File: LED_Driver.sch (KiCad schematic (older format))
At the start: 6 parts

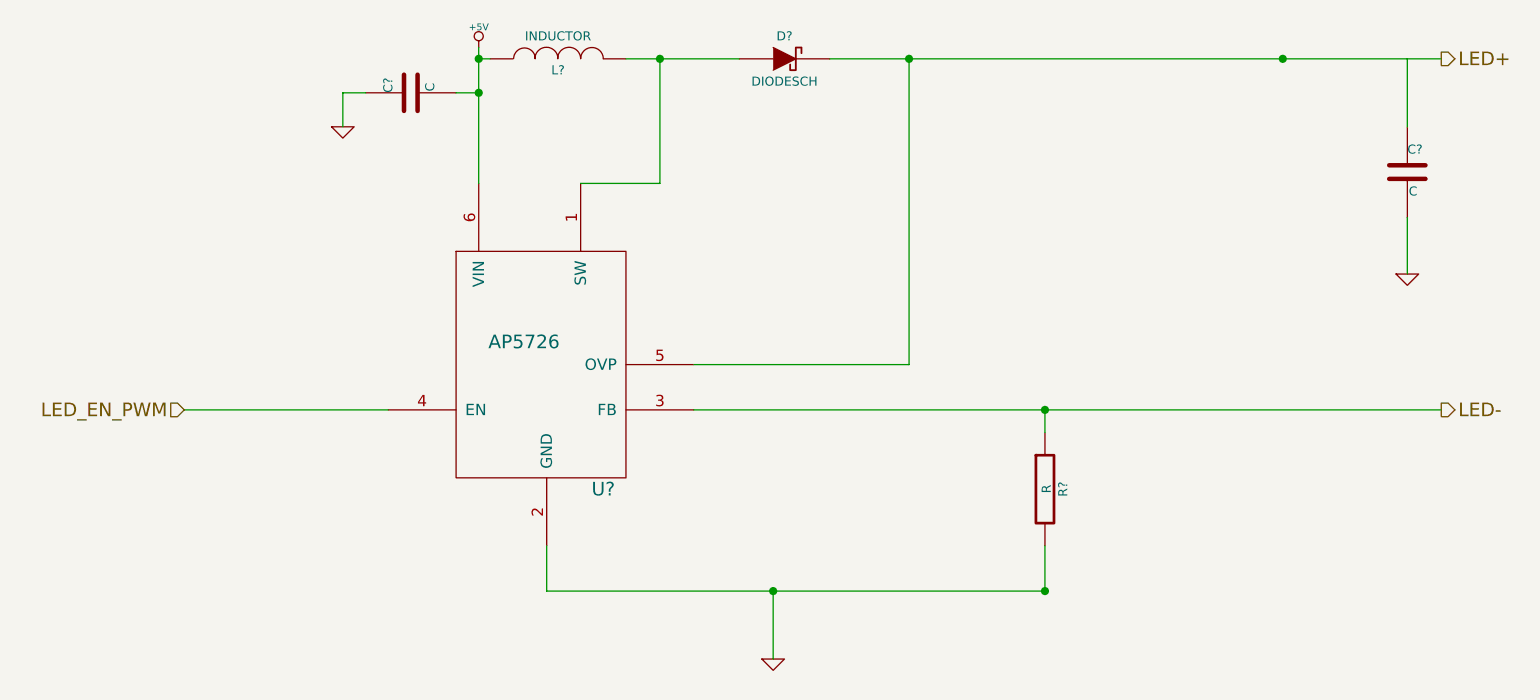
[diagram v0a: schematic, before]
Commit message: RELAY 02-20-2014
1) Created and associated footprints for relay module
2) Placed relay module's components in PCB layout
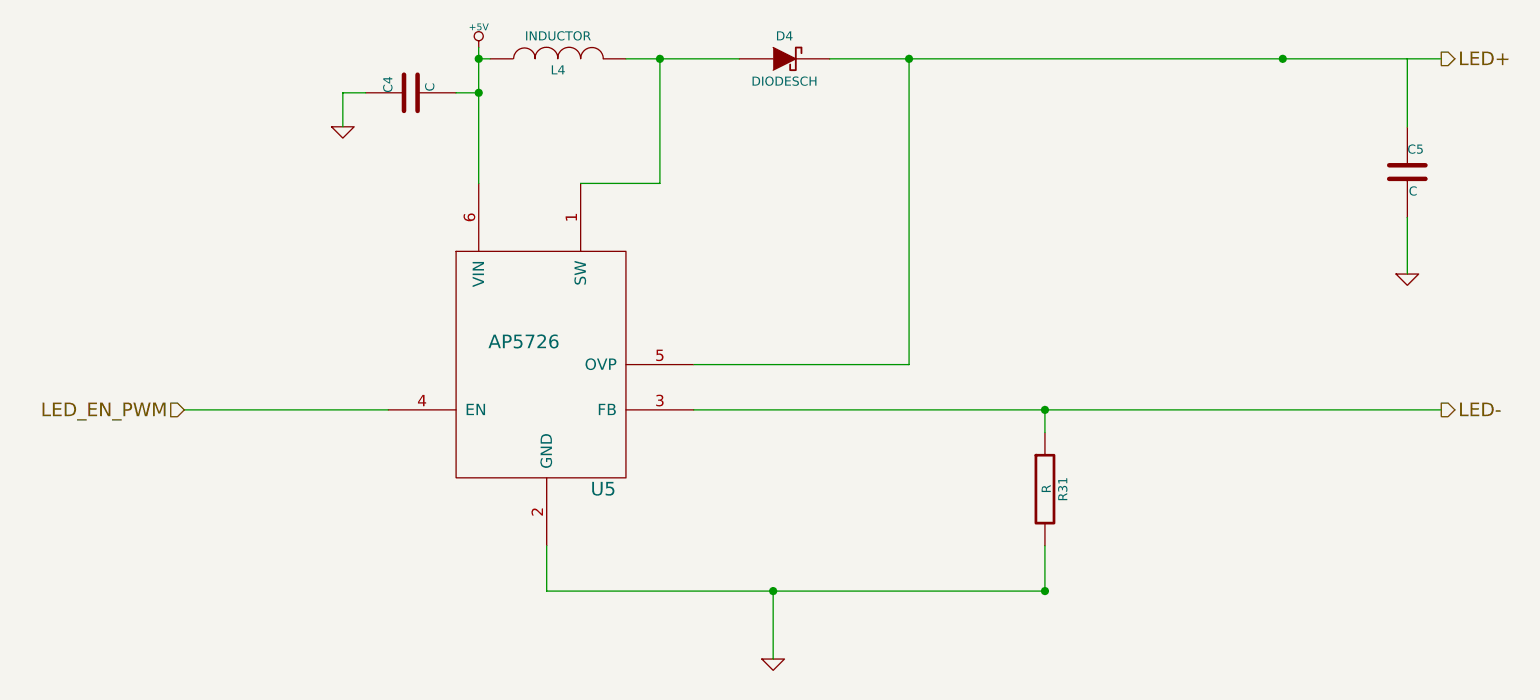
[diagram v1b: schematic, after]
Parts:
- gave numbers to parts that had none: 6
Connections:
- wire segments 27 -> 20
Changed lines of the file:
@@
 Sheet 5 9
 Title ""
-Date "11 feb 2014"
+Date "20 feb 2014"
 Rev ""
 Comp ""
@@
 LED-
 $Comp
-L AP5726 U?
+L AP5726 U5
 U 1 1 52F8483D
 P 4600 2800
-F 0 "U?" H 4950 2350 60  0000 C CNN
+F 0 "U5" H 4950 2350 60  0000 C CNN
 F 1 "AP5726" H 4600 3000 60  0000 C CNN
 F 2 "" H 4600 2800 60  0000 C CNN
@@
 	3100 2900 4000 2900
 $Comp
-L +5V #PWR?
+L +5V #PWR34
 U 1 1 52F84ACD
 P 4400 1300
-F 0 "#PWR?" H 4400 1390 20  0001 C CNN
+F 0 "#PWR34" H 4400 1390 20  0001 C CNN
 F 1 "+5V" H 4400 1390 30  0000 C CNN
 F 2 "" H 4400 1300 60  0000 C CNN
@@
 $EndComp
 $Comp
-L GND #PWR?
+L GND #PWR33
 U 1 1 52F84ADC
 P 3800 1650
-F 0 "#PWR?" H 3800 1650 30  0001 C CNN
+F 0 "#PWR33" H 3800 1650 30  0001 C CNN
 F 1 "GND" H 3800 1580 30  0001 C CNN
 F 2 "" H 3800 1650 60  0000 C CNN
@@
 $EndComp
 Wire Wire Line
-	4400 1300 4400 1350
-Wire Wire Line
-	4400 1350 4400 1500
-Wire Wire Line
-	4400 1500 4400 1900
+	4400 1300 4400 1900
 $Comp
-L C C?
+L C C4
 U 1 1 52F84B01
 P 4100 1500
-F 0 "C?" H 4100 1600 40  0000 L CNN
+F 0 "C4" H 4100 1600 40  0000 L CNN
 F 1 "C" H 4106 1415 40  0000 L CNN
 F 2 "~" H 4138 1350 30  0000 C CNN
@@
 	3800 1500 3800 1650
 $Comp
-L INDUCTOR L?
+L INDUCTOR L4
 U 1 1 52F84B22
 P 4750 1350
-F 0 "L?" V 4700 1350 40  0000 C CNN
+F 0 "L4" V 4700 1350 40  0000 C CNN
 F 1 "INDUCTOR" V 4850 1350 40  0000 C CNN
 F 2 "~" H 4750 1350 60  0000 C CNN
@@
 Connection ~ 4400 1350
 Wire Wire Line
-	5050 1350 5200 1350
-Wire Wire Line
-	5200 1350 5550 1350
+	5050 1350 5550 1350
 Wire Wire Line
 	5200 1350 5200 1900
@@
 	5200 1900 4850 1900
 $Comp
-L DIODESCH D?
+L DIODESCH D4
 U 1 1 52F84B4A
 P 5750 1350
-F 0 "D?" H 5750 1450 40  0000 C CNN
+F 0 "D4" H 5750 1450 40  0000 C CNN
 F 1 "DIODESCH" H 5750 1250 40  0000 C CNN
 F 2 "~" H 5750 1350 60  0000 C CNN
@@
 	6300 2700 6300 1350
 Wire Wire Line
-	5950 1350 6300 1350
-Wire Wire Line
-	6300 1350 7950 1350
-Wire Wire Line
-	7950 1350 8650 1350
+	5950 1350 8650 1350
 $Comp
-L R R?
+L R R31
 U 1 1 52F84B73
 P 6900 3250
-F 0 "R?" V 6980 3250 40  0000 C CNN
+F 0 "R31" V 6980 3250 40  0000 C CNN
 F 1 "R" V 6907 3251 40  0000 C CNN
 F 2 "~" V 6830 3250 30  0000 C CNN
@@
 $EndComp
 Wire Wire Line
-	5350 2900 6900 2900
-Wire Wire Line
-	6900 2900 8650 2900
+	5350 2900 8650 2900
 Wire Wire Line
 	6900 2900 6900 3000
@@
 	6900 3700 6900 3500
 $Comp
-L C C?
+L C C5
 U 1 1 52F84BA7
 P 8500 1850
-F 0 "C?" H 8500 1950 40  0000 L CNN
+F 0 "C5" H 8500 1950 40  0000 L CNN
 F 1 "C" H 8506 1765 40  0000 L CNN
 F 2 "~" H 8538 1700 30  0000 C CNN
@@
 Connection ~ 6300 1350
 $Comp
-L GND #PWR?
+L GND #PWR35
 U 1 1 52F84BE2
 P 5700 4000
-F 0 "#PWR?" H 5700 4000 30  0001 C CNN
+F 0 "#PWR35" H 5700 4000 30  0001 C CNN
 F 1 "GND" H 5700 3930 30  0001 C CNN
 F 2 "" H 5700 4000 60  0000 C CNN
@@
 Connection ~ 7950 1350
 $Comp
-L GND #PWR?
+L GND #PWR36
 U 1 1 52F84C43
 P 8500 2300
-F 0 "#PWR?" H 8500 2300 30  0001 C CNN
+F 0 "#PWR36" H 8500 2300 30  0001 C CNN
 F 1 "GND" H 8500 2230 30  0001 C CNN
 F 2 "" H 8500 2300 60  0000 C CNN
@@
 	8500 2300 8500 2050
 Wire Wire Line
-	4700 3700 5700 3700
-Wire Wire Line
-	5700 3700 6900 3700
+	4700 3700 6900 3700
 Connection ~ 6900 2900
 $EndSCHEMATC

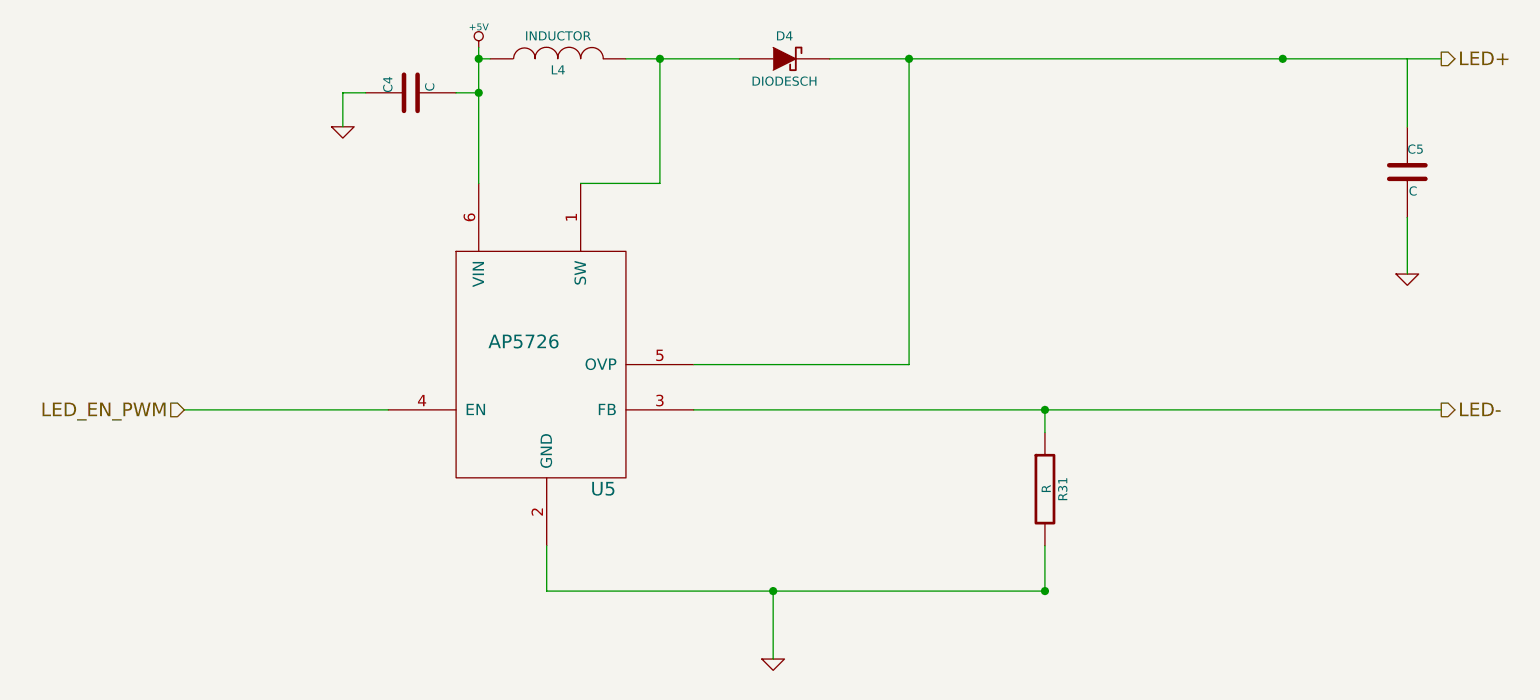
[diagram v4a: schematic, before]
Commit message: Completed placement and association of all footprints
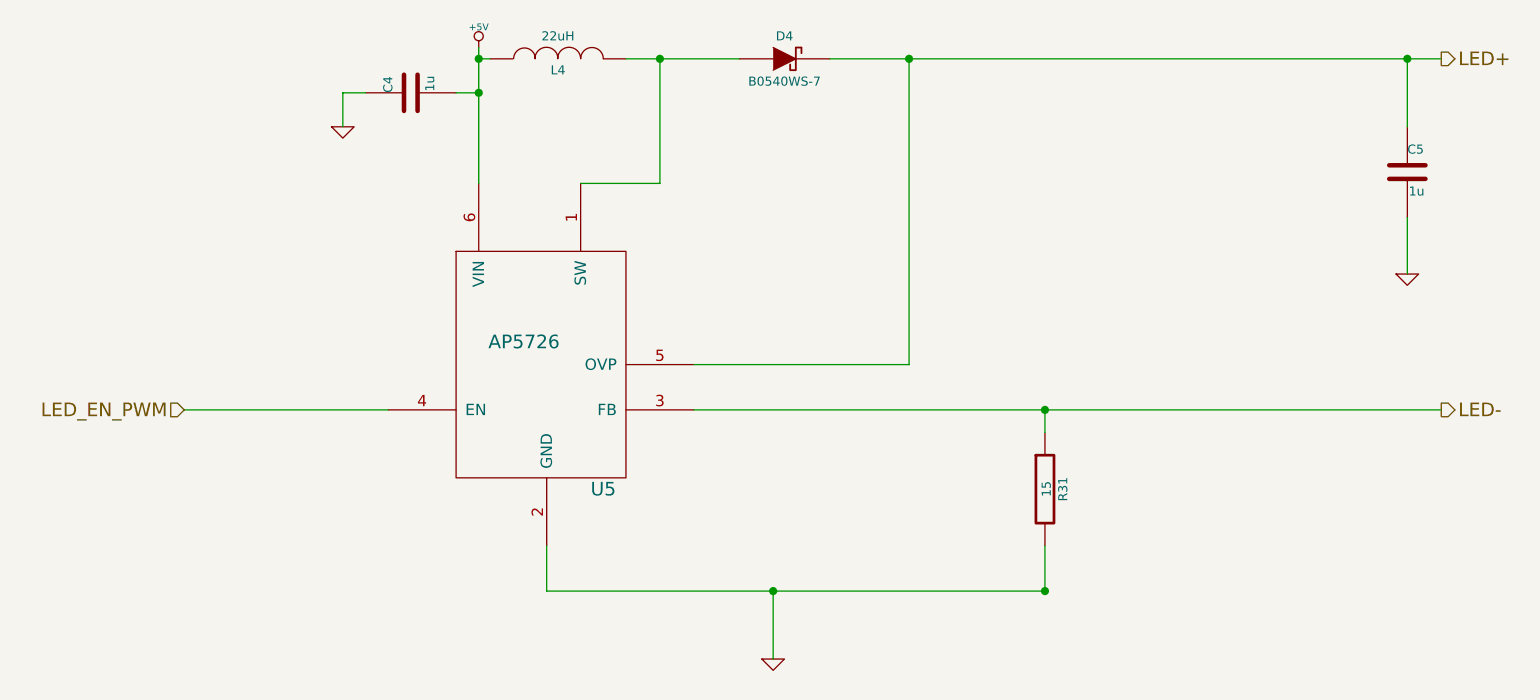
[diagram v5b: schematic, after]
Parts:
- C4, C5: value C -> 1u
- D4: value DIODESCH -> B0540WS-7; MFG NAME (none) -> Diodes Incorporated; MFG PART NUM (none) -> B0540WS-7
- L4: value INDUCTOR -> 22uH; MFG NAME (none) -> Taiyo Yuden; MFG PART NUM (none) -> NR4012T220M
- R31: value R -> 15
- U5: MFG NAME (none) -> Diodes Incorporated; MFG PART NUM (none) -> AP5726WG-7
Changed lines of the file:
@@
 Sheet 5 9
 Title ""
-Date "25 feb 2014"
+Date "28 feb 2014"
 Rev ""
 Comp ""
@@
 F 2 "" H 4600 2800 60  0000 C CNN
 F 3 "" H 4600 2800 60  0000 C CNN
+F 4 "Diodes Incorporated" H 4600 2800 60  0001 C CNN "MFG NAME"
+F 5 "AP5726WG-7" H 4600 2800 60  0001 C CNN "MFG PART NUM"
 	1    4600 2800
 	1    0    0    -1
@@
 P 4100 1500
 F 0 "C4" H 4100 1600 40  0000 L CNN
-F 1 "C" H 4106 1415 40  0000 L CNN
+F 1 "1u" H 4106 1415 40  0000 L CNN
 F 2 "~" H 4138 1350 30  0000 C CNN
 F 3 "~" H 4100 1500 60  0000 C CNN
@@
 P 4750 1350
 F 0 "L4" V 4700 1350 40  0000 C CNN
-F 1 "INDUCTOR" V 4850 1350 40  0000 C CNN
+F 1 "22uH" V 4850 1350 40  0000 C CNN
 F 2 "~" H 4750 1350 60  0000 C CNN
 F 3 "~" H 4750 1350 60  0000 C CNN
+F 4 "Taiyo Yuden" H 4750 1350 60  0001 C CNN "MFG NAME"
+F 5 "NR4012T220M" H 4750 1350 60  0001 C CNN "MFG PART NUM"
 	1    4750 1350
 	0    -1   -1   0
@@
 P 5750 1350
 F 0 "D4" H 5750 1450 40  0000 C CNN
-F 1 "DIODESCH" H 5750 1250 40  0000 C CNN
+F 1 "B0540WS-7" H 5750 1250 40  0000 C CNN
 F 2 "~" H 5750 1350 60  0000 C CNN
 F 3 "~" H 5750 1350 60  0000 C CNN
+F 4 "Diodes Incorporated" H 5750 1350 60  0001 C CNN "MFG NAME"
+F 5 "B0540WS-7" H 5750 1350 60  0001 C CNN "MFG PART NUM"
 	1    5750 1350
 	1    0    0    -1
@@
 P 6900 3250
 F 0 "R31" V 6980 3250 40  0000 C CNN
-F 1 "R" V 6907 3251 40  0000 C CNN
+F 1 "15" V 6907 3251 40  0000 C CNN
 F 2 "~" V 6830 3250 30  0000 C CNN
 F 3 "~" H 6900 3250 30  0000 C CNN
@@
 P 8500 1850
 F 0 "C5" H 8500 1950 40  0000 L CNN
-F 1 "C" H 8506 1765 40  0000 L CNN
+F 1 "1u" H 8506 1765 40  0000 L CNN
 F 2 "~" H 8538 1700 30  0000 C CNN
 F 3 "~" H 8500 1850 60  0000 C CNN
@@
 $EndComp
 Connection ~ 6900 3700
-Wire Wire Line
-	8500 1350 8500 1650
 Connection ~ 6300 1350
 $Comp
@@
 	5700 4000 5700 3700
 Connection ~ 5700 3700
-Connection ~ 7950 1350
 $Comp
 L GND #PWR043
@@
 	4700 3700 6900 3700
 Connection ~ 6900 2900
+Wire Wire Line
+	8500 1650 8500 1350
+Connection ~ 8500 1350
 $EndSCHEMATC

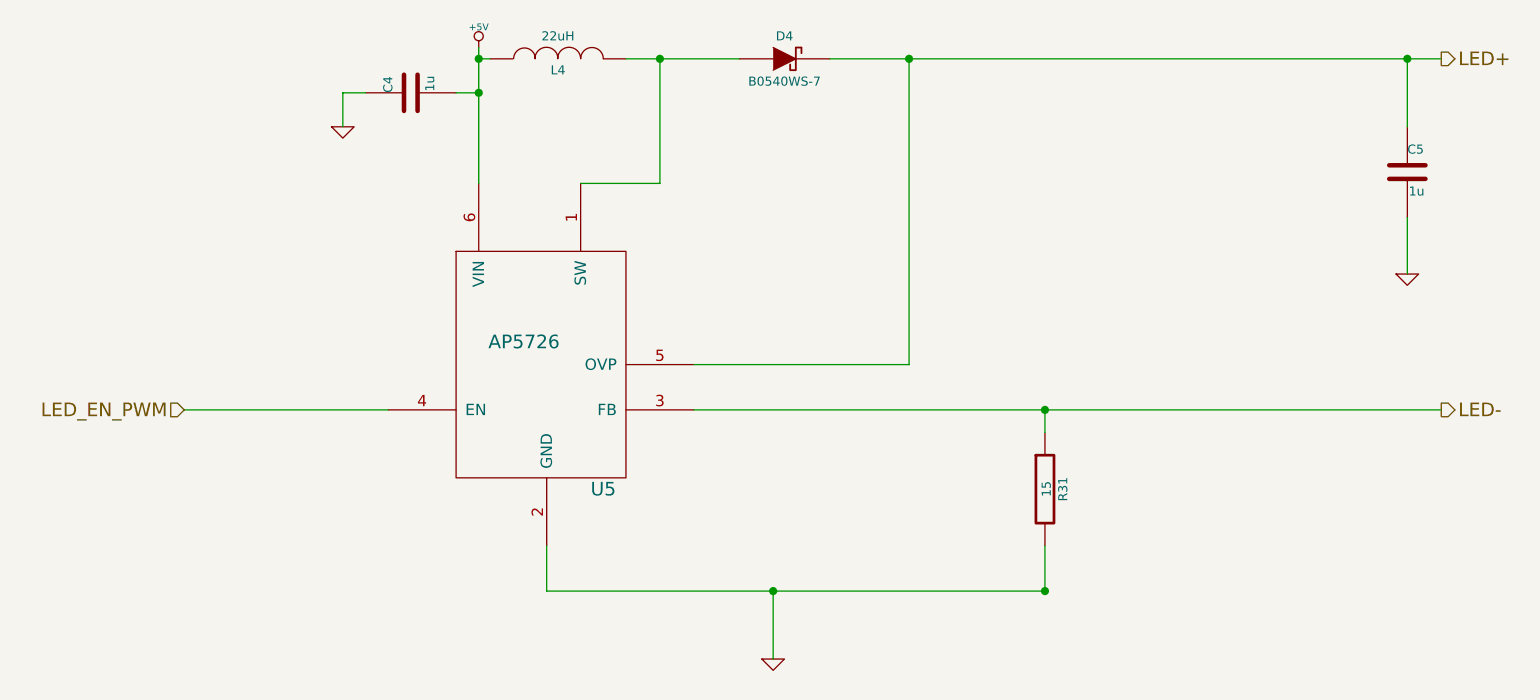
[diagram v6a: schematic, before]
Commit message: Layout v4.0
Adding ground planes according to location of modules
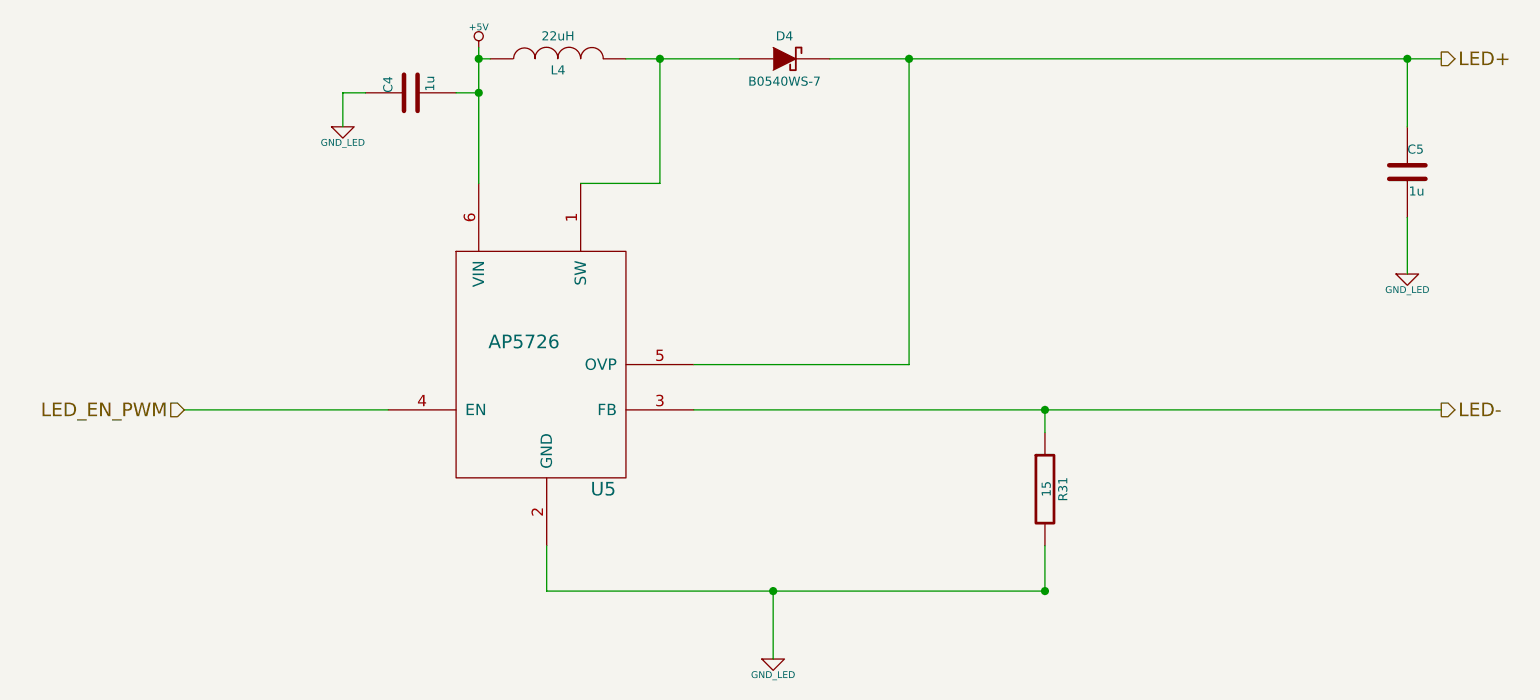
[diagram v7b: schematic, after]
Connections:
- net GND renamed GND_LED
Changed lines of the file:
@@
 Sheet 5 9
 Title ""
-Date "3 mar 2014"
+Date "6 mar 2014"
 Rev ""
 Comp ""
@@
 F 3 "" H 4400 1300 60  0000 C CNN
 	1    4400 1300
-	1    0    0    -1
-$EndComp
-$Comp
-L GND #PWR038
-U 1 1 52F84ADC
-P 3800 1650
-F 0 "#PWR038" H 3800 1650 30  0001 C CNN
-F 1 "GND" H 3800 1580 30  0001 C CNN
-F 2 "" H 3800 1650 60  0000 C CNN
-F 3 "" H 3800 1650 60  0000 C CNN
-	1    3800 1650
 	1    0    0    -1
 $EndComp
@@
 Connection ~ 6900 3700
 Connection ~ 6300 1350
-$Comp
-L GND #PWR039
-U 1 1 52F84BE2
-P 5700 4000
-F 0 "#PWR039" H 5700 4000 30  0001 C CNN
-F 1 "GND" H 5700 3930 30  0001 C CNN
-F 2 "" H 5700 4000 60  0000 C CNN
-F 3 "" H 5700 4000 60  0000 C CNN
-	1    5700 4000
-	1    0    0    -1
-$EndComp
 Wire Wire Line
 	5700 4000 5700 3700
 Connection ~ 5700 3700
-$Comp
-L GND #PWR040
-U 1 1 52F84C43
-P 8500 2300
-F 0 "#PWR040" H 8500 2300 30  0001 C CNN
-F 1 "GND" H 8500 2230 30  0001 C CNN
-F 2 "" H 8500 2300 60  0000 C CNN
-F 3 "" H 8500 2300 60  0000 C CNN
-	1    8500 2300
-	1    0    0    -1
-$EndComp
 Wire Wire Line
 	8500 2300 8500 2050
@@
 	8500 1650 8500 1350
 Connection ~ 8500 1350
+$Comp
+L GND_LED #PWR038
+U 1 1 5318400D
+P 5700 4000
+F 0 "#PWR038" H 5700 4000 30  0001 C CNN
+F 1 "GND_LED" H 5700 3930 30  0000 C CNN
+F 2 "" H 5700 4000 60  0000 C CNN
+F 3 "" H 5700 4000 60  0000 C CNN
+	1    5700 4000
+	1    0    0    -1
+$EndComp
+$Comp
+L GND_LED #PWR039
+U 1 1 5318401C
+P 3800 1650
+F 0 "#PWR039" H 3800 1650 30  0001 C CNN
+F 1 "GND_LED" H 3800 1580 30  0000 C CNN
+F 2 "" H 3800 1650 60  0000 C CNN
+F 3 "" H 3800 1650 60  0000 C CNN
+	1    3800 1650
+	1    0    0    -1
+$EndComp
+$Comp
+L GND_LED #PWR040
+U 1 1 5318402B
+P 8500 2300
+F 0 "#PWR040" H 8500 2300 30  0001 C CNN
+F 1 "GND_LED" H 8500 2230 30  0000 C CNN
+F 2 "" H 8500 2300 60  0000 C CNN
+F 3 "" H 8500 2300 60  0000 C CNN
+	1    8500 2300
+	1    0    0    -1
+$EndComp
 $EndSCHEMATC

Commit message: Layout v5.0
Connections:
- net +5V renamed +5P
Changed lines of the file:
@@
 Sheet 5 9
 Title ""
-Date "6 mar 2014"
+Date "8 mar 2014"
 Rev ""
 Comp ""
@@
 Wire Wire Line
 	3100 2900 4000 2900
-$Comp
-L +5V #PWR037
-U 1 1 52F84ACD
-P 4400 1300
-F 0 "#PWR037" H 4400 1390 20  0001 C CNN
-F 1 "+5V" H 4400 1390 30  0000 C CNN
-F 2 "" H 4400 1300 60  0000 C CNN
-F 3 "" H 4400 1300 60  0000 C CNN
-	1    4400 1300
-	1    0    0    -1
-$EndComp
 Wire Wire Line
 	4400 1300 4400 1900
@@
 	1    0    0    -1
 $EndComp
+$Comp
+L +5P #PWR44
+U 1 1 53199C69
+P 4400 1300
+F 0 "#PWR44" H 4400 1430 20  0001 C CNN
+F 1 "+5P" H 4400 1400 30  0000 C CNN
+F 2 "" H 4400 1300 60  0000 C CNN
+F 3 "" H 4400 1300 60  0000 C CNN
+	1    4400 1300
+	1    0    0    -1
+$EndComp
